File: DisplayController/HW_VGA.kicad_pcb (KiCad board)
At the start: 2 copper layers, 150 x 90 mm, 77 parts, among them J1 Conn_02x40_Odd_Even, J301 Conn_01x02, J401 Conn_01x06, U102 GAL22V10, U103 74ALS163, U104 74ALS163, U105 74ALS163, U202 GAL22V10, U203 74ALS163, U204 74ALS163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

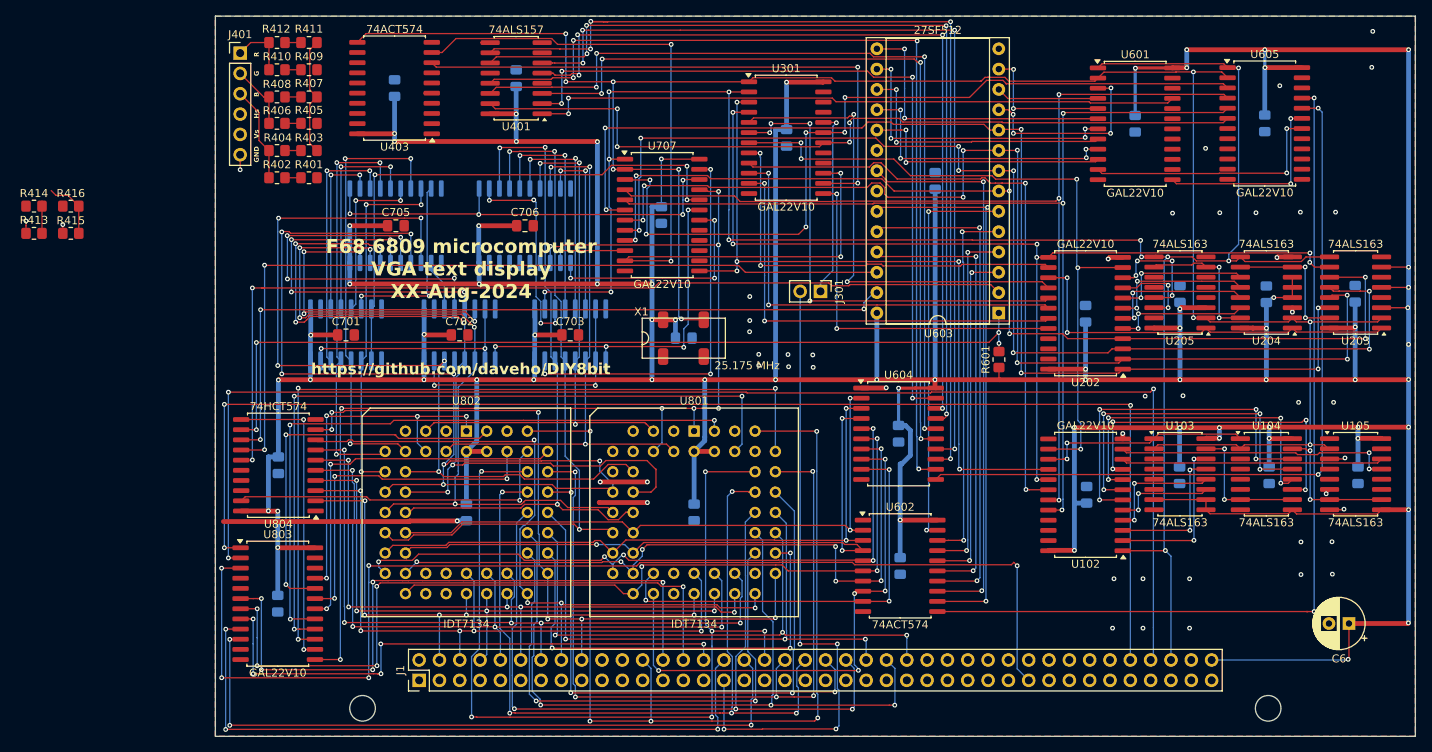
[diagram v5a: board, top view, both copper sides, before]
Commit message: routed VSync/HSync output voltage dividers
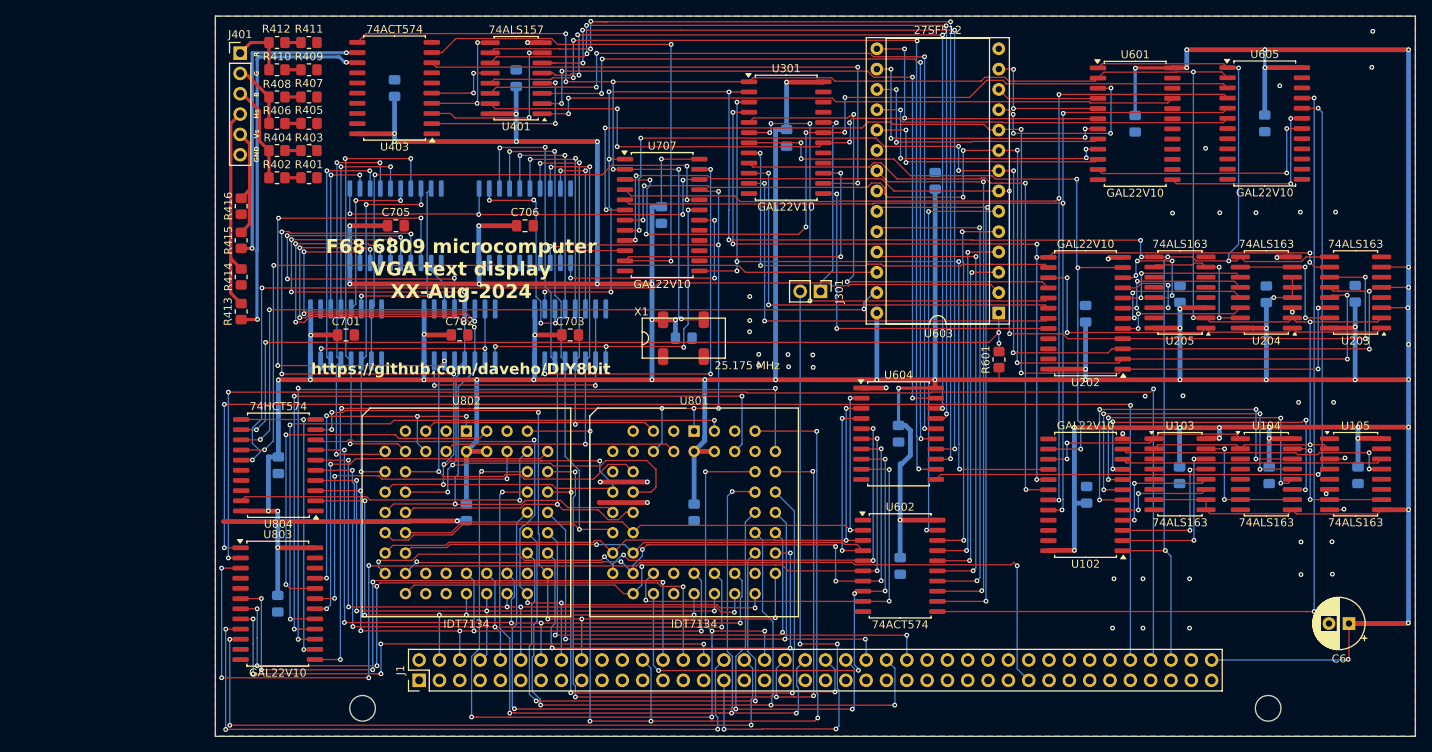
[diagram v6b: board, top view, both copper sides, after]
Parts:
- moved R413 27.7 mm to (66.7, 95.3), turned to 90 degrees
- moved R414 27.4 mm to (66.7, 91.0), turned to -90 degrees
- moved R415 21.3 mm to (66.7, 86.4), turned to 90 degrees
- moved R416 21.3 mm to (66.7, 82.2), turned to -90 degrees
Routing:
- net Net-(U403-Q6): track 1.55 -> 47.7 mm, vias 1 -> 2
- net Net-(U403-Q7): track 1.10 -> 39.0 mm, vias 1 -> 2
- net /Output/HSyncOut: track 4.05 -> 26.6 mm
- net Net-(U401-Za): track 1.12 -> 23.4 mm, vias 0 -> 2
- net Net-(U401-Zb): track 0.00 -> 22.2 mm, vias 0 -> 2
- net /Output/Intense: track 15.0 -> 1.27 mm
- net Net-(U401-Zc): track 1.20 -> 14.9 mm, vias 0 -> 2
- net Net-(U401-Zd): track 1.76 -> 10.8 mm, vias 0 -> 2
- net /Output/VSyncOut: track 7.66 -> 14.7 mm
- net /FontA13: track 102.9 -> 102.2 mm
- net /FontA15: track 111.0 -> 110.3 mm
- net /FontA14: track 97.0 -> 96.4 mm

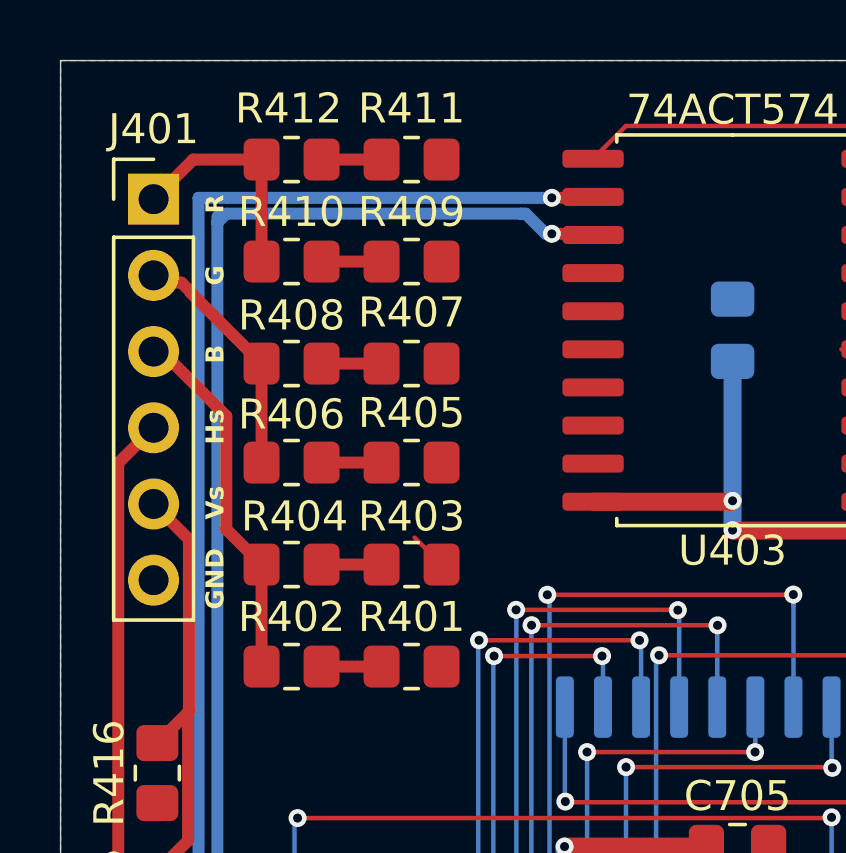
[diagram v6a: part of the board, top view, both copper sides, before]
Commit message: finished all of the rats nest wires I can see
There are still unrouted nets, which are probably grounded
pins connected to an isolated fill area. This should be
resolvable by adding vias to connect the top and bottom
layer ground planes (hopefully.)
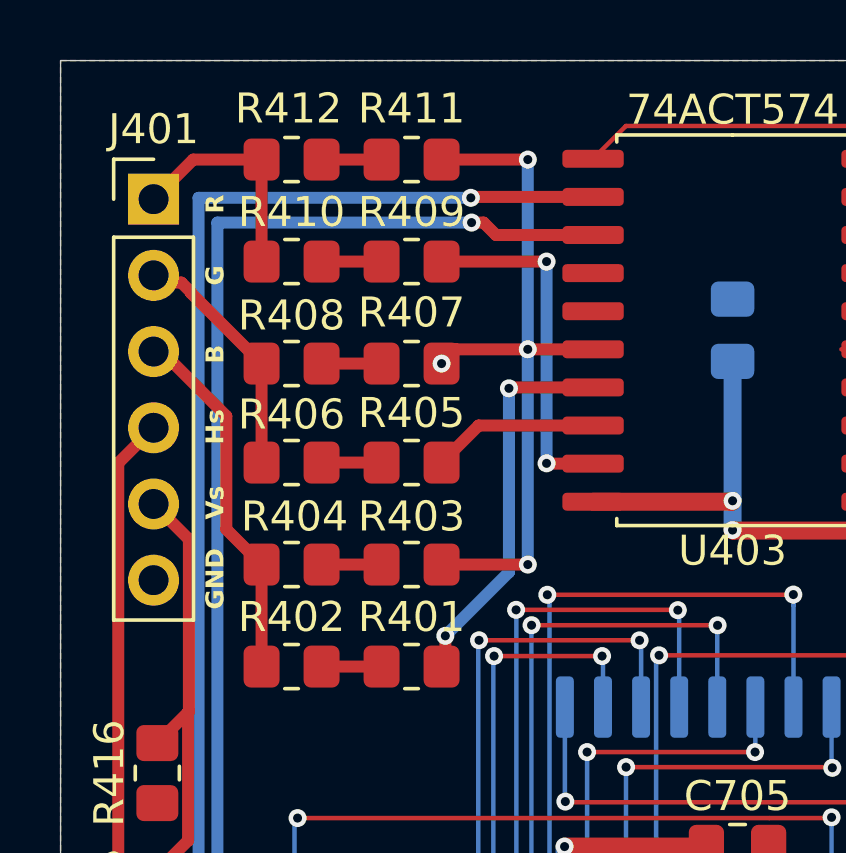
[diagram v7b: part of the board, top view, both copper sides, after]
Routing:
- net /Output/Intense: track 1.27 -> 24.6 mm, vias 0 -> 4
- net /Output/Blue: track 0.00 -> 13.0 mm, vias 0 -> 2
- net /Output/Red: track 0.00 -> 11.8 mm, vias 0 -> 2
- net /Output/Green: track 0.00 -> 5.56 mm
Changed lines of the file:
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@@
 	)
 	(segment
-		(start 75.3 74.3)
+		(start 81.25 69.295)
+		(end 78.476 69.295)
+		(width 0.4)
+		(layer "F.Cu")
+		(net 88)
+	)
+	(segment
+		(start 76.325 78.475)
+		(end 76.2 78.6)
+		(width 0.4)
+		(layer "F.Cu")
+		(net 88)
+	)
+	(segment
+		(start 76.325 77.575)
+		(end 76.325 78.475)
+		(width 0.4)
+		(layer "F.Cu")
+		(net 88)
+	)
+	(segment
+		(start 78.476 69.295)
+		(end 78.446 69.325)
+		(width 0.4)
+		(layer "F.Cu")
+		(net 88)
+	)
+	(via
+		(at 78.446 69.325)
+		(size 0.6)
+		(drill 0.3)
+		(layers "F.Cu" "B.Cu")
+		(net 88)
+	)
+	(via
+		(at 76.325 77.575)
+		(size 0.6)
+		(drill 0.3)
+		(layers "F.Cu" "B.Cu")
+		(net 88)
+	)
+	(segment
+		(start 78.446 69.325)
+		(end 78.446 75.454)
+		(width 0.4)
+		(layer "B.Cu")
+		(net 88)
+	)
+	(segment
+		(start 78.446 75.454)
+		(end 76.325 77.575)
+		(width 0.4)
+		(layer "B.Cu")
+		(net 88)
+	)
+	(segment
+		(start 81.25 68.025)
+		(end 79.175 68.025)
+		(width 0.4)
+		(layer "F.Cu")
+		(net 89)
+	)
+	(segment
+		(start 79.075 61.7)
+		(end 76.2 61.7)
+		(width 0.4)
+		(layer "F.Cu")
+		(net 89)
+	)
+	(segment
+		(start 79.175 68.025)
+		(end 79.073 68.025)
+		(width 0.4)
+		(layer "F.Cu")
+		(net 89)
+	)
+	(segment
+		(start 79.175 68.025)
+		(end 76.675 68.025)
+		(width 0.4)
+		(layer "F.Cu")
+		(net 89)
+	)
+	(segment
+		(start 76.675 68.025)
+		(end 76.2 68.5)
+		(width 0.4)
+		(layer "F.Cu")
+		(net 89)
+	)
+	(segment
+		(start 79.075 75.2)
 		(end 76.2 75.2)
-		(width 0.15)
-		(layer "F.Cu")
+		(width 0.4)
+		(layer "F.Cu")
+		(net 89)
+	)
+	(via
+		(at 79.073 68.025)
+		(size 0.6)
+		(drill 0.3)
+		(layers "F.Cu" "B.Cu")
+		(net 89)
+	)
+	(via
+		(at 79.075 61.7)
+		(size 0.6)
+		(drill 0.3)
+		(layers "F.Cu" "B.Cu")
+		(net 89)
+	)
+	(via
+		(at 79.075 75.2)
+		(size 0.6)
+		(drill 0.3)
+		(layers "F.Cu" "B.Cu")
+		(net 89)
+	)
+	(via
+		(at 76.2 68.5)
+		(size 0.6)
+		(drill 0.3)
+		(layers "F.Cu" "B.Cu")
+		(net 89)
+	)
+	(segment
+		(start 79.073 68.025)
+		(end 79.073 75.198)
+		(width 0.4)
+		(layer "B.Cu")
+		(net 89)
+	)
+	(segment
+		(start 79.073 61.702)
+		(end 79.075 61.7)
+		(width 0.4)
+		(layer "B.Cu")
+		(net 89)
+	)
+	(segment
+		(start 79.073 75.198)
+		(end 79.075 75.2)
+		(width 0.4)
+		(layer "B.Cu")
+		(net 89)
+	)
+	(segment
+		(start 79.073 68.025)
+		(end 79.073 61.702)
+		(width 0.4)
+		(layer "B.Cu")
 		(net 89)
 	)
@@
 	)
 	(segment
+		(start 77.435 70.565)
+		(end 76.2 71.8)
+		(width 0.4)
+		(layer "F.Cu")
+		(net 92)
+	)
+	(segment
+		(start 81.25 70.565)
+		(end 77.435 70.565)
+		(width 0.4)
+		(layer "F.Cu")
+		(net 92)
+	)
+	(segment
 		(start 72.2 68.5)
 		(end 74.2 68.5)
@@
 	)
 	(segment
+		(start 79.71 71.835)
+		(end 79.7 71.825)
+		(width 0.4)
+		(layer "F.Cu")
+		(net 94)
+	)
+	(segment
+		(start 81.25 71.835)
+		(end 79.71 71.835)
+		(width 0.4)
+		(layer "F.Cu")
+		(net 94)
+	)
+	(segment
+		(start 79.7 65.1)
+		(end 76.2 65.1)
+		(width 0.4)
+		(layer "F.Cu")
+		(net 94)
+	)
+	(via
+		(at 79.7 65.1)
+		(size 0.6)
+		(drill 0.3)
+		(layers "F.Cu" "B.Cu")
+		(net 94)
+	)
+	(via
+		(at 79.7 71.825)
+		(size 0.6)
+		(drill 0.3)
+		(layers "F.Cu" "B.Cu")
+		(net 94)
+	)
+	(segment
+		(start 79.7 71.825)
+		(end 79.7 65.1)
+		(width 0.4)
+		(layer "B.Cu")
+		(net 94)
+	)
+	(segment
 		(start 72.2 65.1)
 		(end 74.2 65.1)
@@
 	)
 	(segment
+		(start 78.015 64.215)
+		(end 81.25 64.215)
+		(width 0.4)
+		(layer "F.Cu")
+		(net 97)
+	)
+	(segment
 		(start 81.21 64.175)
 		(end 81.25 64.215)
@@
 	)
 	(segment
-		(start 79.875 64.175)
-		(end 81.21 64.175)
+		(start 77.2 63.8)
+		(end 77.6 63.8)
 		(width 0.4)
 		(layer "F.Cu")
@@
 		(net 97)
 	)
-	(via
-		(at 79.875 64.175)
+	(segment
+		(start 77.6 63.8)
+		(end 78.015 64.215)
+		(width 0.4)
+		(layer "F.Cu")
+		(net 97)
+	)
+	(via
+		(at 77.2 63.8)
 		(size 0.6)
 		(drill 0.3)
@@
 	(segment
 		(start 68.727 63.8)
-		(end 69.025 63.502)
+		(end 77.2 63.8)
 		(width 0.4)
 		(layer "B.Cu")
@@
 	)
 	(segment
-		(start 68.727 63.8)
-		(end 68.727 63.602)
-		(width 0.4)
-		(layer "B.Cu")
-		(net 97)
-	)
-	(segment
-		(start 79.002 63.502)
-		(end 79.675 64.175)
-		(width 0.4)
-		(layer "B.Cu")
-		(net 97)
-	)
-	(segment
 		(start 68.698 87.713712)
 		(end 68.727 87.684712)
@@
 	)
 	(segment
-		(start 78.85 63.502)
-		(end 79.002 63.502)
-		(width 0.4)
-		(layer "B.Cu")
-		(net 97)
-	)
-	(segment
 		(start 68.773 96.3)
 		(end 68.698 96.225)
@@
 	)
 	(segment
-		(start 69.025 63.502)
-		(end 78.85 63.502)
-		(width 0.4)
-		(layer "B.Cu")
-		(net 97)
-	)
-	(segment
-		(start 79.675 64.175)
-		(end 79.875 64.175)
-		(width 0.4)
-		(layer "B.Cu")
-		(net 97)
-	)
-	(segment
-		(start 79.875 62.975)
-		(end 81.22 62.975)
+		(start 77.205 62.945)
+		(end 81.25 62.945)
 		(width 0.4)
 		(layer "F.Cu")
@@
 		(net 98)
 	)
-	(via
-		(at 79.875 62.975)
-		(size 0.6)
-		(drill 0.3)
-		(layers "F.Cu" "B.Cu")
+	(segment
+		(start 77.175 62.975)
+		(end 77.205 62.945)
+		(width 0.4)
+		(layer "F.Cu")
 		(net 98)
 	)
@@
 		(net 98)
 	)
+	(via
+		(at 77.175 62.975)
+		(size 0.6)
+		(drill 0.3)
+		(layers "F.Cu" "B.Cu")
+		(net 98)
+	)
 	(segment
 		(start 68.1 62.975)
-		(end 79.875 62.975)
-		(width 0.4)
-		(layer "B.Cu")
+		(end 77.175 62.975)
+		(width 0.4)
+		(layer "B.Cu")
